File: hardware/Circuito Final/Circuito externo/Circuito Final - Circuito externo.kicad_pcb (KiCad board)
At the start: 2 copper layers, 121 x 100.5 mm, 14 parts, among them J1 Conn_02x19_Odd_Even, J2 Conn_02x19_Odd_Even, J3 Conn_01x02, J4 Conn_01x02, SW1 SW_SPDT, SW2 SW_DIP_x04

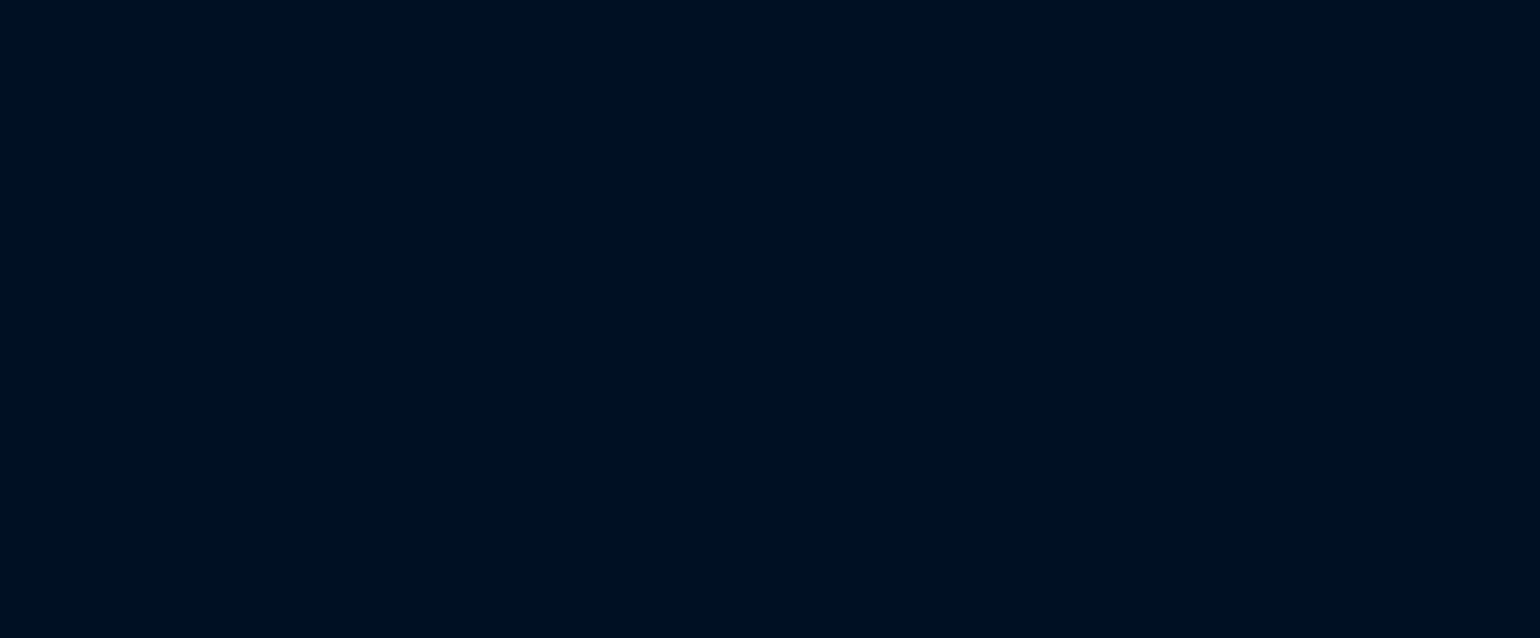
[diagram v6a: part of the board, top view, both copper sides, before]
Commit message: update del pcb del circuito central y subida de bitacora del 24 de junio
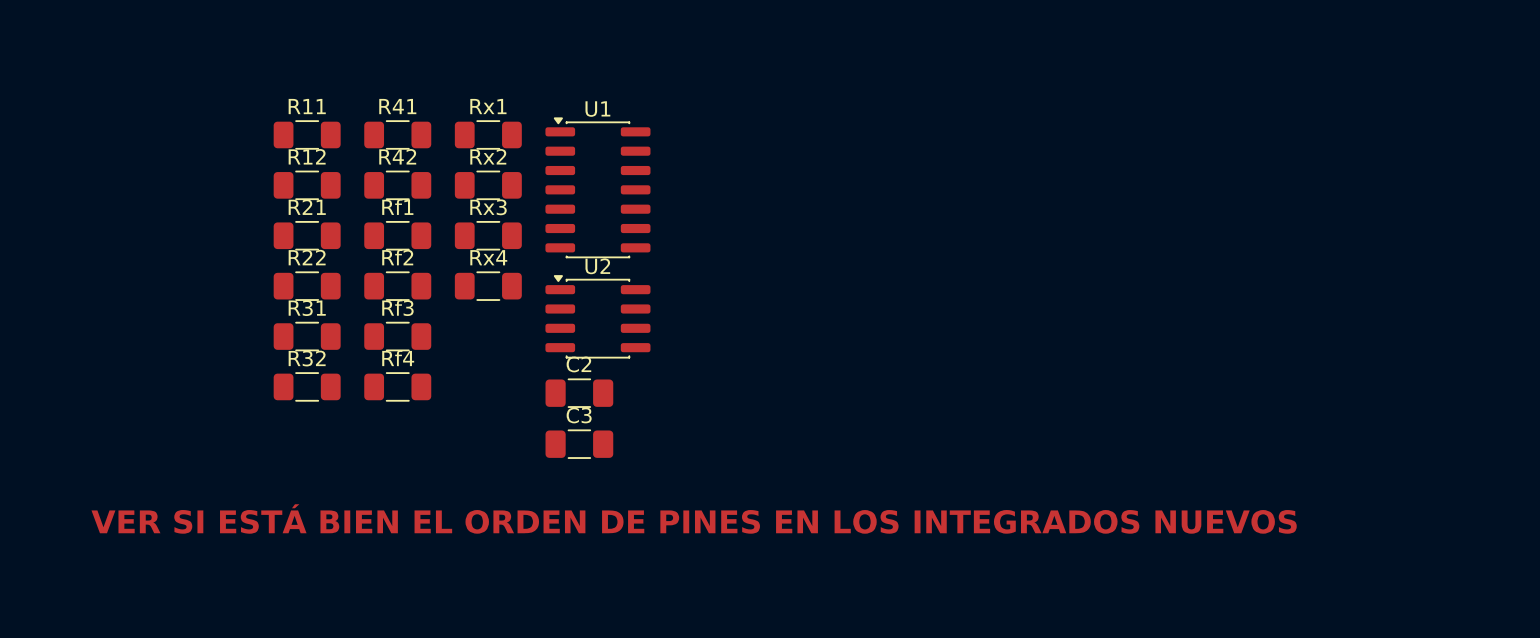
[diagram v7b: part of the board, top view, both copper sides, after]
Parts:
- added C2: 10u, Capacitor_SMD:C_1206_3216Metric_Pad1.33x1.80mm_HandSolder, F.Cu at (212.9, 108.8)
- added C3: 10u, Capacitor_SMD:C_1206_3216Metric_Pad1.33x1.80mm_HandSolder, F.Cu at (212.9, 112.2)
- added R11: 39k, Resistor_SMD:R_1206_3216Metric_Pad1.30x1.75mm_HandSolder, F.Cu at (195.0, 91.9)
- added R12: 39k, Resistor_SMD:R_1206_3216Metric_Pad1.30x1.75mm_HandSolder, F.Cu at (195.0, 95.2)
- added R21: 39k, Resistor_SMD:R_1206_3216Metric_Pad1.30x1.75mm_HandSolder, F.Cu at (195.0, 98.5)
- added R22: 39k, Resistor_SMD:R_1206_3216Metric_Pad1.30x1.75mm_HandSolder, F.Cu at (195.0, 101.8)
- added R31: 39k, Resistor_SMD:R_1206_3216Metric_Pad1.30x1.75mm_HandSolder, F.Cu at (195.0, 105.1)
- added R32: 39k, Resistor_SMD:R_1206_3216Metric_Pad1.30x1.75mm_HandSolder, F.Cu at (195.0, 108.4)
- added R41: 39k, Resistor_SMD:R_1206_3216Metric_Pad1.30x1.75mm_HandSolder, F.Cu at (200.9, 91.9)
- added R42: 39k, Resistor_SMD:R_1206_3216Metric_Pad1.30x1.75mm_HandSolder, F.Cu at (200.9, 95.2)
- added Rf1: 33k, Resistor_SMD:R_1206_3216Metric_Pad1.30x1.75mm_HandSolder, F.Cu at (200.9, 98.5)
- added Rf2: 33k, Resistor_SMD:R_1206_3216Metric_Pad1.30x1.75mm_HandSolder, F.Cu at (200.9, 101.8)
- added Rf3: 33k, Resistor_SMD:R_1206_3216Metric_Pad1.30x1.75mm_HandSolder, F.Cu at (200.9, 105.1)
- added Rf4: 33k, Resistor_SMD:R_1206_3216Metric_Pad1.30x1.75mm_HandSolder, F.Cu at (200.9, 108.4)
- added Rx1: 33k, Resistor_SMD:R_1206_3216Metric_Pad1.30x1.75mm_HandSolder, F.Cu at (206.9, 91.9)
- added Rx2: 33k, Resistor_SMD:R_1206_3216Metric_Pad1.30x1.75mm_HandSolder, F.Cu at (206.9, 95.2)
- added Rx3: 33k, Resistor_SMD:R_1206_3216Metric_Pad1.30x1.75mm_HandSolder, F.Cu at (206.9, 98.5)
- added Rx4: 33k, Resistor_SMD:R_1206_3216Metric_Pad1.30x1.75mm_HandSolder, F.Cu at (206.9, 101.8)
- added U1: Opamp_Quad, Package_SO:SO-14_3.9x8.65mm_P1.27mm, F.Cu at (214.1, 95.5)
- added U2: ICL7660, Package_SO:SOIC-8_3.9x4.9mm_P1.27mm, F.Cu at (214.1, 103.9)
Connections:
- J1 pad 29: /bus_pos_1 -> /bus_pos_1_med
- J1 pad 31: /bus_neg_1 -> /bus_neg_1_med
- J1 pad 35: /bus_neg_2 -> unconnected-(J1-Pin_35-Pad35)
- J1 pad 37: /bus_neg_3 -> unconnected-(J1-Pin_37-Pad37)
- J1 pad 38: /bus_pos_2 -> /bus_pos_2_med
- J2 pad 12: /bus_pos_4 -> /bus_pos_4_med
- J2 pad 14: /bus_neg_4 -> unconnected-(J2-Pin_14-Pad14)
- J2 pad 16: /bus_pos_3 -> /bus_pos_3_med
- Jsalida_2 pad 7: /bus_neg_2 -> /bus_pos_1
- Jsalida_2 pad 8: /bus_neg_2 -> /bus_pos_1
- Jsalida_3 pad 7: /bus_neg_3 -> /bus_pos_2
- Jsalida_3 pad 8: /bus_neg_3 -> /bus_pos_2
- Jsalida_4 pad 7: /bus_neg_4 -> /bus_pos_3
- Jsalida_4 pad 8: /bus_neg_4 -> /bus_pos_3
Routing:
- net /bus_pos_2: track 97.6 -> 229.2 mm, vias 0 -> 4
- net /bus_neg_3: track 131.6 -> 0.00 mm, vias 4 -> 0
- net /bus_neg_2: track 64.9 -> 0.00 mm, vias 2 -> 0
- net /bus_pos_1: track 131.1 -> 196.0 mm, vias 4 -> 6
- net /bus_neg_4: track 53.7 -> 0.00 mm, vias 2 -> 0
- net /bus_pos_3: track 106.2 -> 159.9 mm, vias 2 -> 4
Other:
- board text added: "VER SI ESTÁ BIEN EL ORDEN DE PINES EN LOS INTEGRADOS NUEVOS"

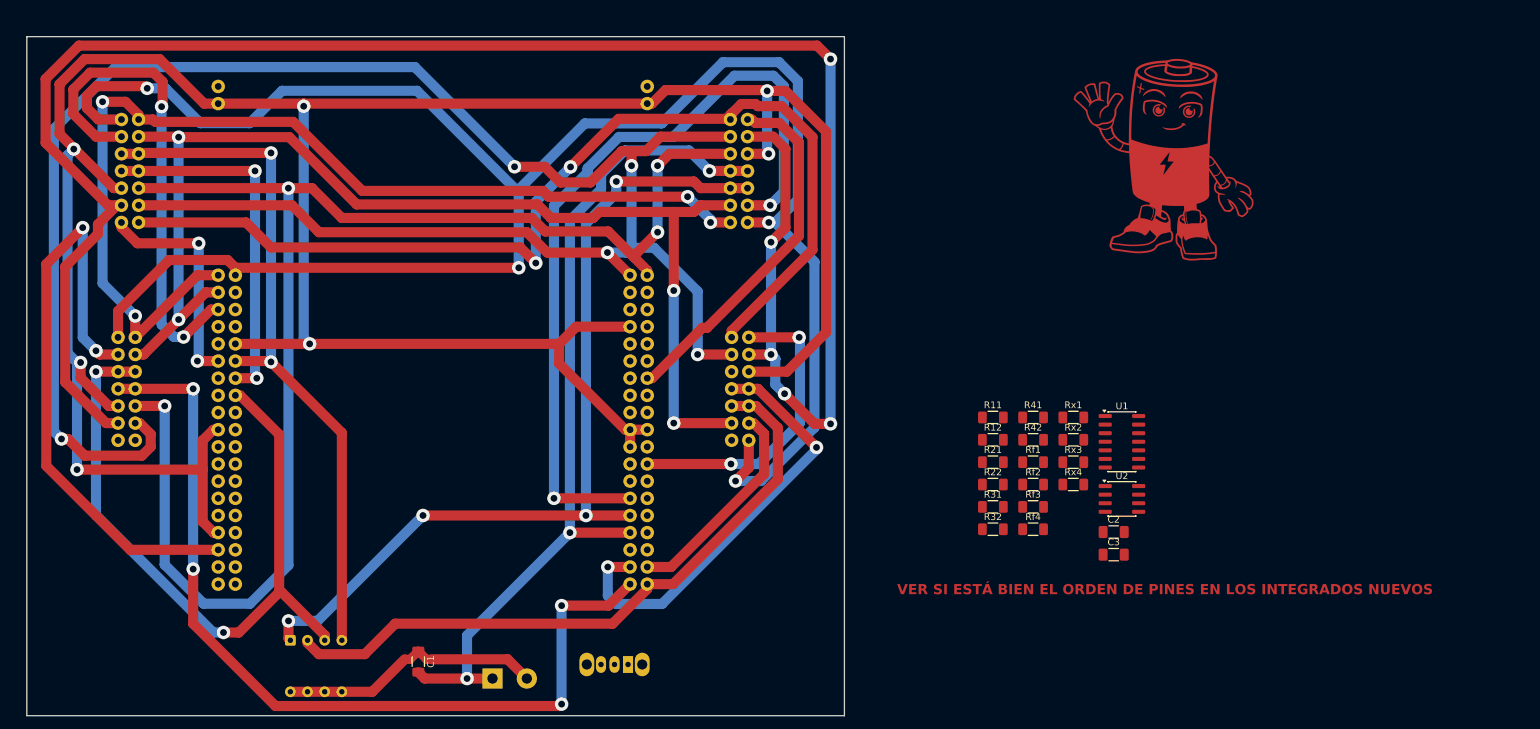
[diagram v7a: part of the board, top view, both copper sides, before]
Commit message: update de esquemático y PCB del circuito externo
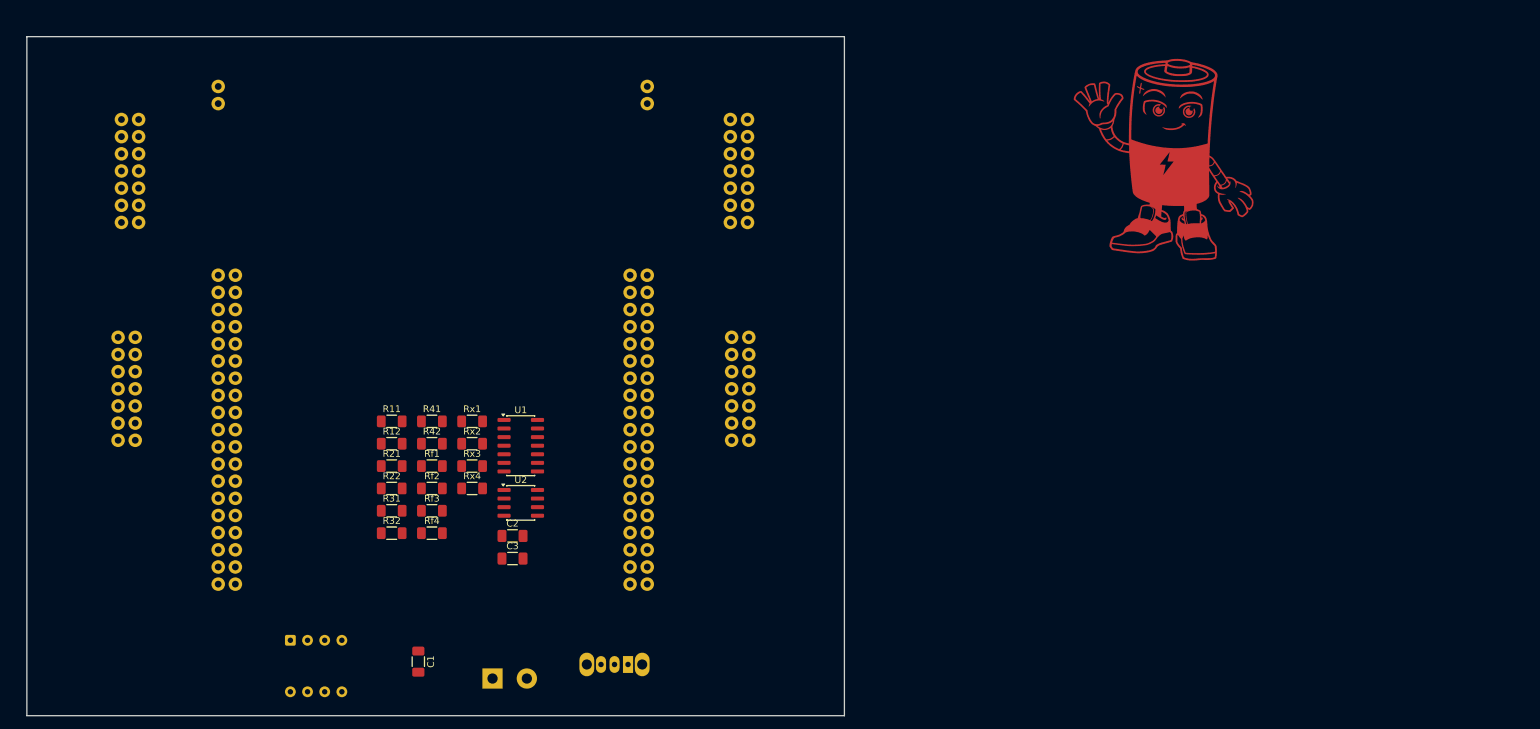
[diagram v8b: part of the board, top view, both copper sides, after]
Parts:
- moved R41 89.0 mm to (112.0, 92.4)
- moved R42 89.0 mm to (112.0, 95.7)
- moved Rf1 89.0 mm to (112.0, 99.1)
- moved Rf2 89.0 mm to (112.0, 102.4)
- moved Rf3 89.0 mm to (112.0, 105.7)
- moved Rf4 89.0 mm to (112.0, 109.0)
- moved C2 89.0 mm to (123.9, 109.4)
- moved C3 89.0 mm to (123.9, 112.7)
- moved R11 89.0 mm to (106.0, 92.4)
- moved R12 89.0 mm to (106.0, 95.7)
- moved R21 89.0 mm to (106.0, 99.1)
- moved R22 89.0 mm to (106.0, 102.4)
- moved R31 89.0 mm to (106.0, 105.7)
- moved R32 89.0 mm to (106.0, 109.0)
- moved Rx1 89.0 mm to (117.9, 92.4)
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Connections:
- J1 pad 29: /bus_pos_1_med -> /banco1_med
- J1 pad 31: /bus_neg_1_med -> unconnected-(J1-Pin_31-Pad31)
- J1 pad 38: /bus_pos_2_med -> /banco2_med
- J2 pad 12: /bus_pos_4_med -> /banco4_med
- J2 pad 16: /bus_pos_3_med -> /banco3_med
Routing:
- net GND: track 410.1 -> 0.00 mm, vias 7 -> 0
- net /clk_latch: track 301.8 -> 0.00 mm, vias 5 -> 0
- net /reset: track 293.8 -> 0.00 mm, vias 5 -> 0
- net /Bit_0: track 293.2 -> 0.00 mm, vias 4 -> 0
- net /bus_pos_2: track 229.2 -> 0.00 mm, vias 4 -> 0
- net /clk_shift: track 214.2 -> 0.00 mm, vias 4 -> 0
- net /bus_pos_1: track 196.0 -> 0.00 mm, vias 6 -> 0
- net /Bit_2: track 176.2 -> 0.00 mm, vias 4 -> 0
- net /bus_pos_3: track 159.9 -> 0.00 mm, vias 4 -> 0
- net /Vcc_out: track 155.1 -> 0.00 mm, vias 2 -> 0
- net /Bit_1: track 153.9 -> 0.00 mm, vias 4 -> 0
- net /bus_neg_1: track 127.5 -> 0.00 mm, vias 3 -> 0
- net /salida_adc_1: track 119.4 -> 0.00 mm, vias 2 -> 0
- net /bus_pos_4: track 104.0 -> 0.00 mm, vias 2 -> 0
- net /salida_adc_3: track 90.6 -> 0.00 mm, vias 2 -> 0
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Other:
- board text removed: "VER SI ESTÁ BIEN EL ORDEN DE PINES EN LOS INTEGRADOS NUEVOS"
